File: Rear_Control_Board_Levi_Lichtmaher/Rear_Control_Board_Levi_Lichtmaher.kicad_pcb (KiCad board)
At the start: 2 copper layers, 142.7 x 84.4 mm, 119 parts, among them J1 430450200, J10 Molex Micro-Fit 4 Pin, J11 22035035, J12 22035035, J13 Conn_01x01_Socket, J14 Conn_01x01_Socket, J2 430450200, J3 430450200, J4 430450200, J5 430450200, J6 430450200, J7 430450200, J8 430450200, J9 22035035, Q1 PSMN1R8-40YLC_115, Q2 PSMN1R8-40YLC_115, Q3 PSMN1R8-40YLC_115, Q4 PSMN1R8-40YLC_115, U11 MCP6286T-E/OT, U12 MCP6286T-E/OT, U2 ADS1118QDGSRQ1, U3 MCP2562-E/P, U4 UA78M05QDCYRG4Q1, U5 ASM330LHHTR, U6 MCP6286T-E/OT

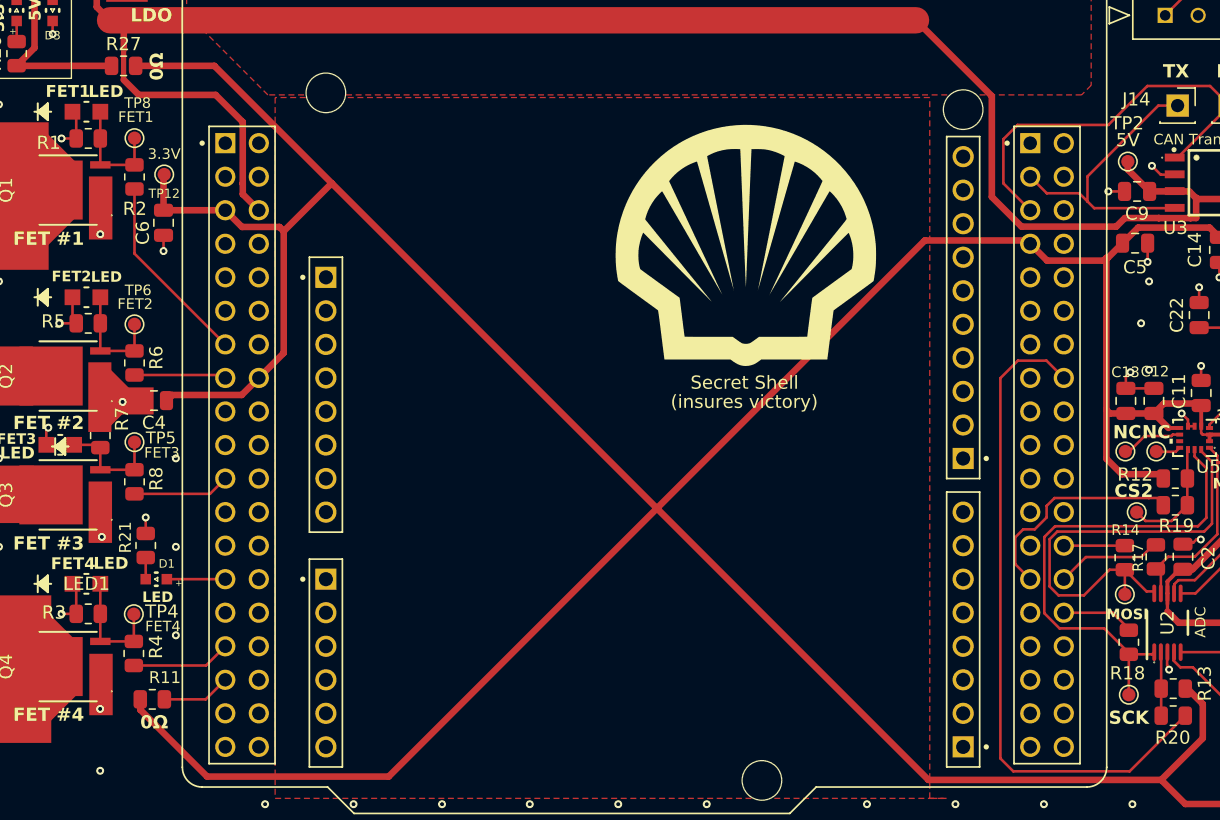
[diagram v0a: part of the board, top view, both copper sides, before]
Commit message: changed a few resistor values
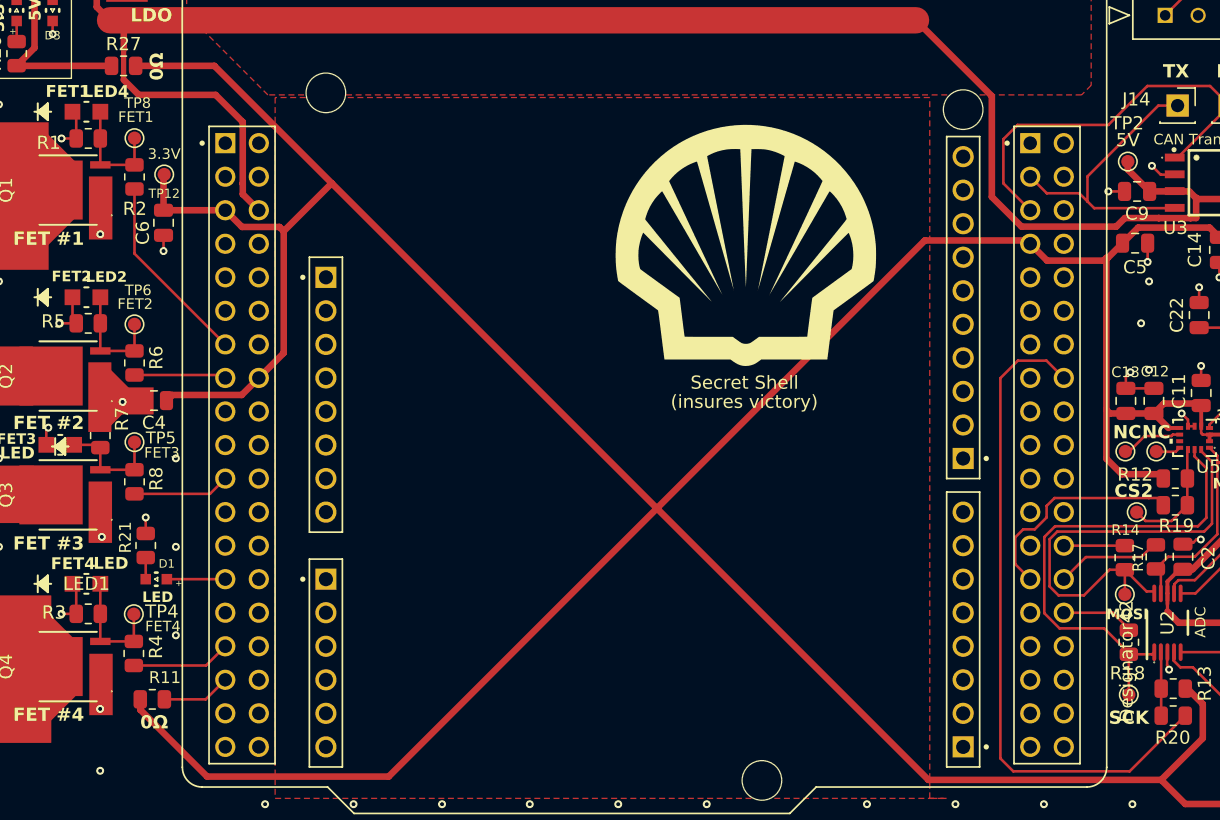
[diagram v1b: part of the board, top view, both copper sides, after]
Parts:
- R22: value 2K -> 20K
- R23: value 1K -> 10K
- renumbered LED to LED2, LED to LED4
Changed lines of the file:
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@@
 			)
 		)
-		(property "Value" "2K"
+		(property "Value" "20K"
 			(at 0 1.65 90)
 			(layer "F.Fab")
@@
 			(layer "F.Fab")
 		)
+		(fp_text user "Designator42"
+			(at -2.921 -3.0988 90)
+			(unlocked yes)
+			(layer "F.SilkS")
+			(effects
+				(font
+					(size 1 1)
+					(thickness 0.15)
+				)
+			)
+		)
 		(fp_text user "${REFERENCE}"
 			(at 0 0 90)
@@
 		(at 98.058401 71.15)
 		(tags "LTST-C170GKT ")
-		(property "Reference" "LED"
+		(property "Reference" "LED4"
 			(at 1.481599 -1.53 0)
 			(unlocked yes)
@@
 		(at 98.058401 85.2)
 		(tags "LTST-C170GKT ")
-		(property "Reference" "LED"
+		(property "Reference" "LED2"
 			(at 1.516599 -1.54 0)
 			(unlocked yes)
@@
 			)
 		)
-		(property "Value" "1K"
+		(property "Value" "10K"
 			(at 0 1.65 90)
 			(layer "F.Fab")

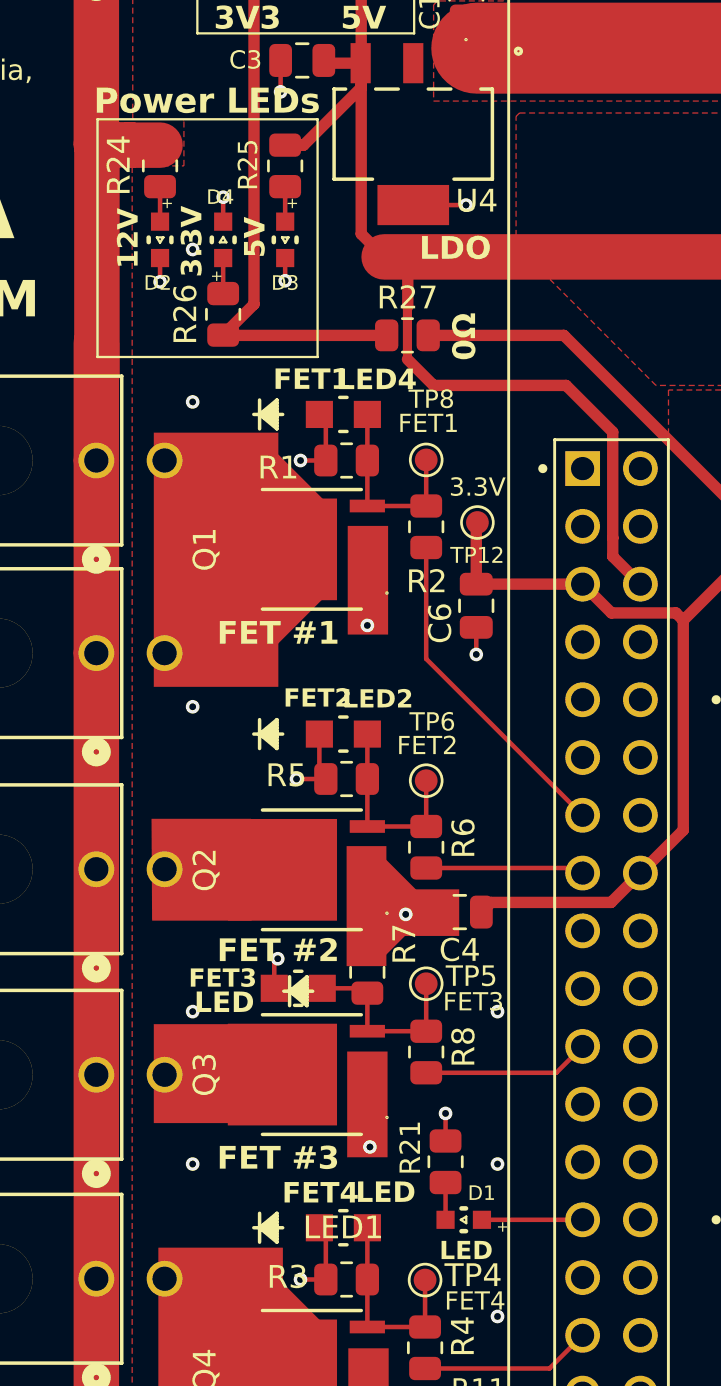
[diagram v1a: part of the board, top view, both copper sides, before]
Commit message: changed led footprint
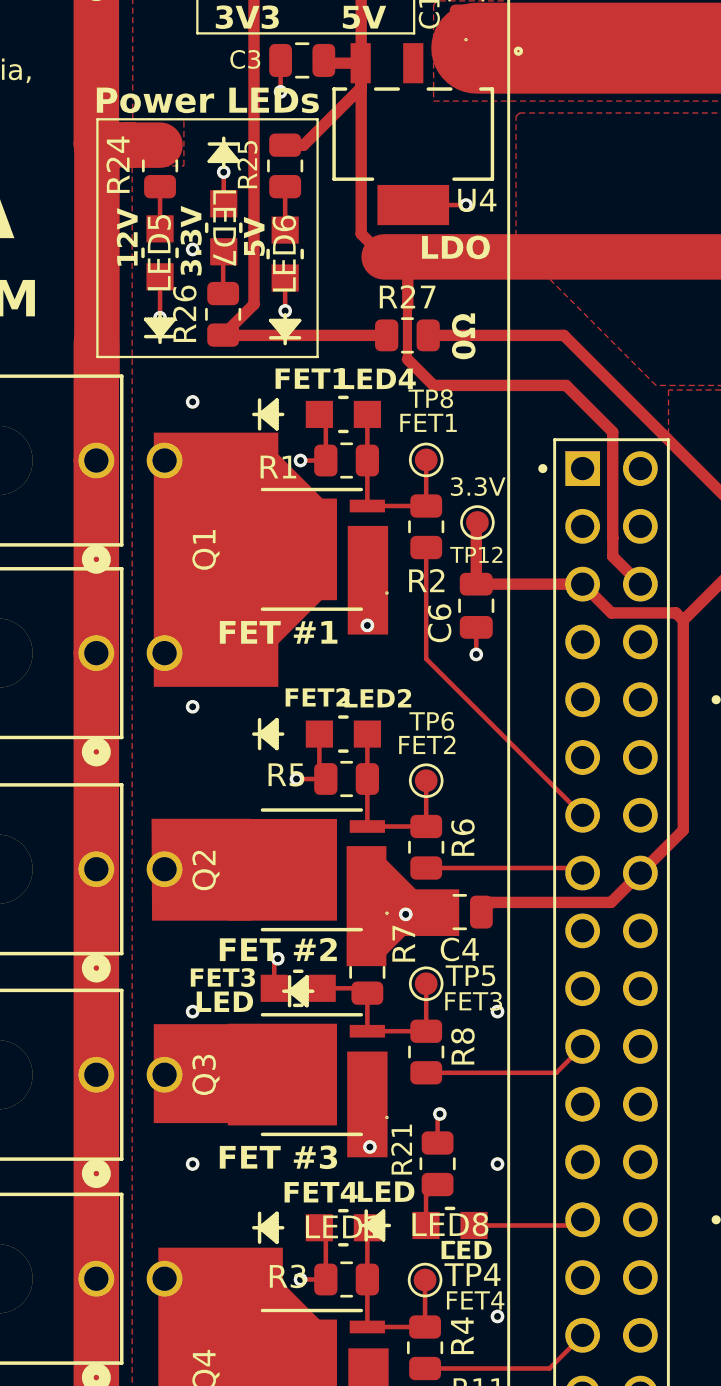
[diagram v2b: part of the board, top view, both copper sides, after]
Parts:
- removed D1, D2, D3, D4: LED, SMV_Passives:WL-SMCW_0603(diode)
- added LED5: LTST-C170GKT, Personal:LED_LTST-C170GKT_LTO, F.Cu at (90.0, 64.0)
- added LED6: LTST-C170GKT, Personal:LED_LTST-C170GKT_LTO, F.Cu at (95.5, 64.1)
- added LED7: LTST-C170GKT, Personal:LED_LTST-C170GKT_LTO, F.Cu at (92.8, 62.9)
- added LED8: LTST-C170GKT, Personal:LED_LTST-C170GKT_LTO, F.Cu at (102.7, 106.8)
- moved R21 0.36 mm to (102.2, 104.1)
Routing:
- net GND: track 82.8 -> 84.5 mm
